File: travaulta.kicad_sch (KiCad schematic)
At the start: 26 parts, among them SW38 BOOT0, U1 STM32F411CCUx, U2 XC6206PxxxMR, Y1 16 MHz

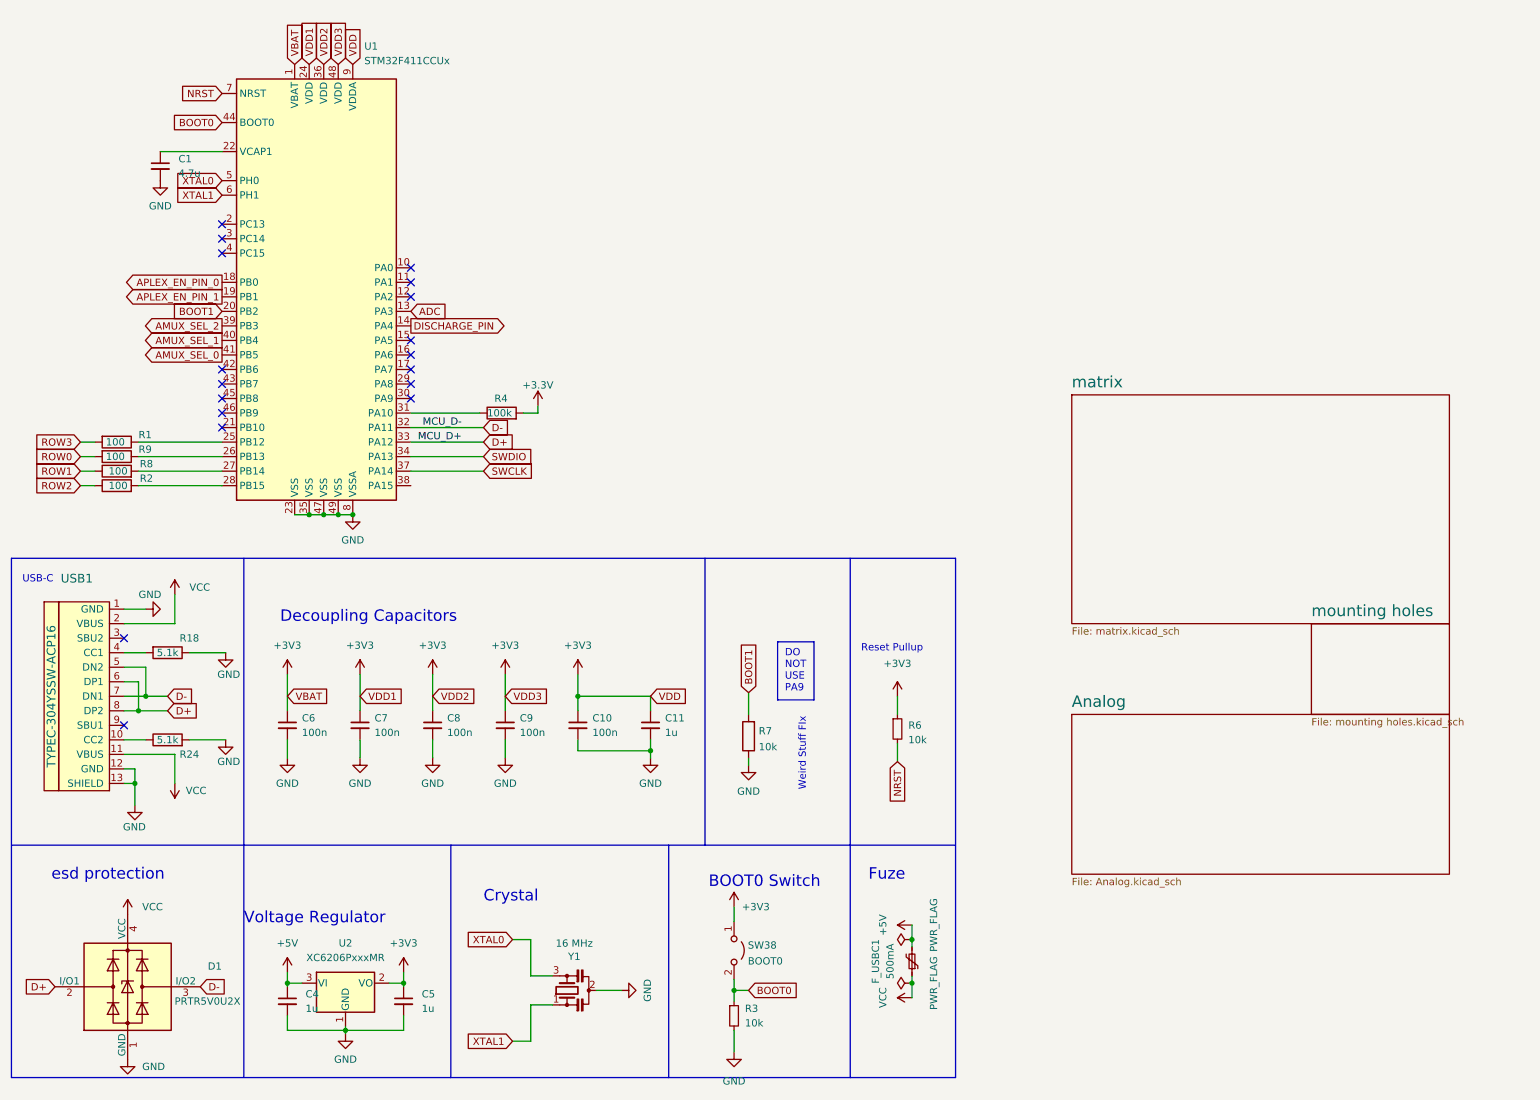
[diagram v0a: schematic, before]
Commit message: MCU swap, UCB components moved, crystal swap
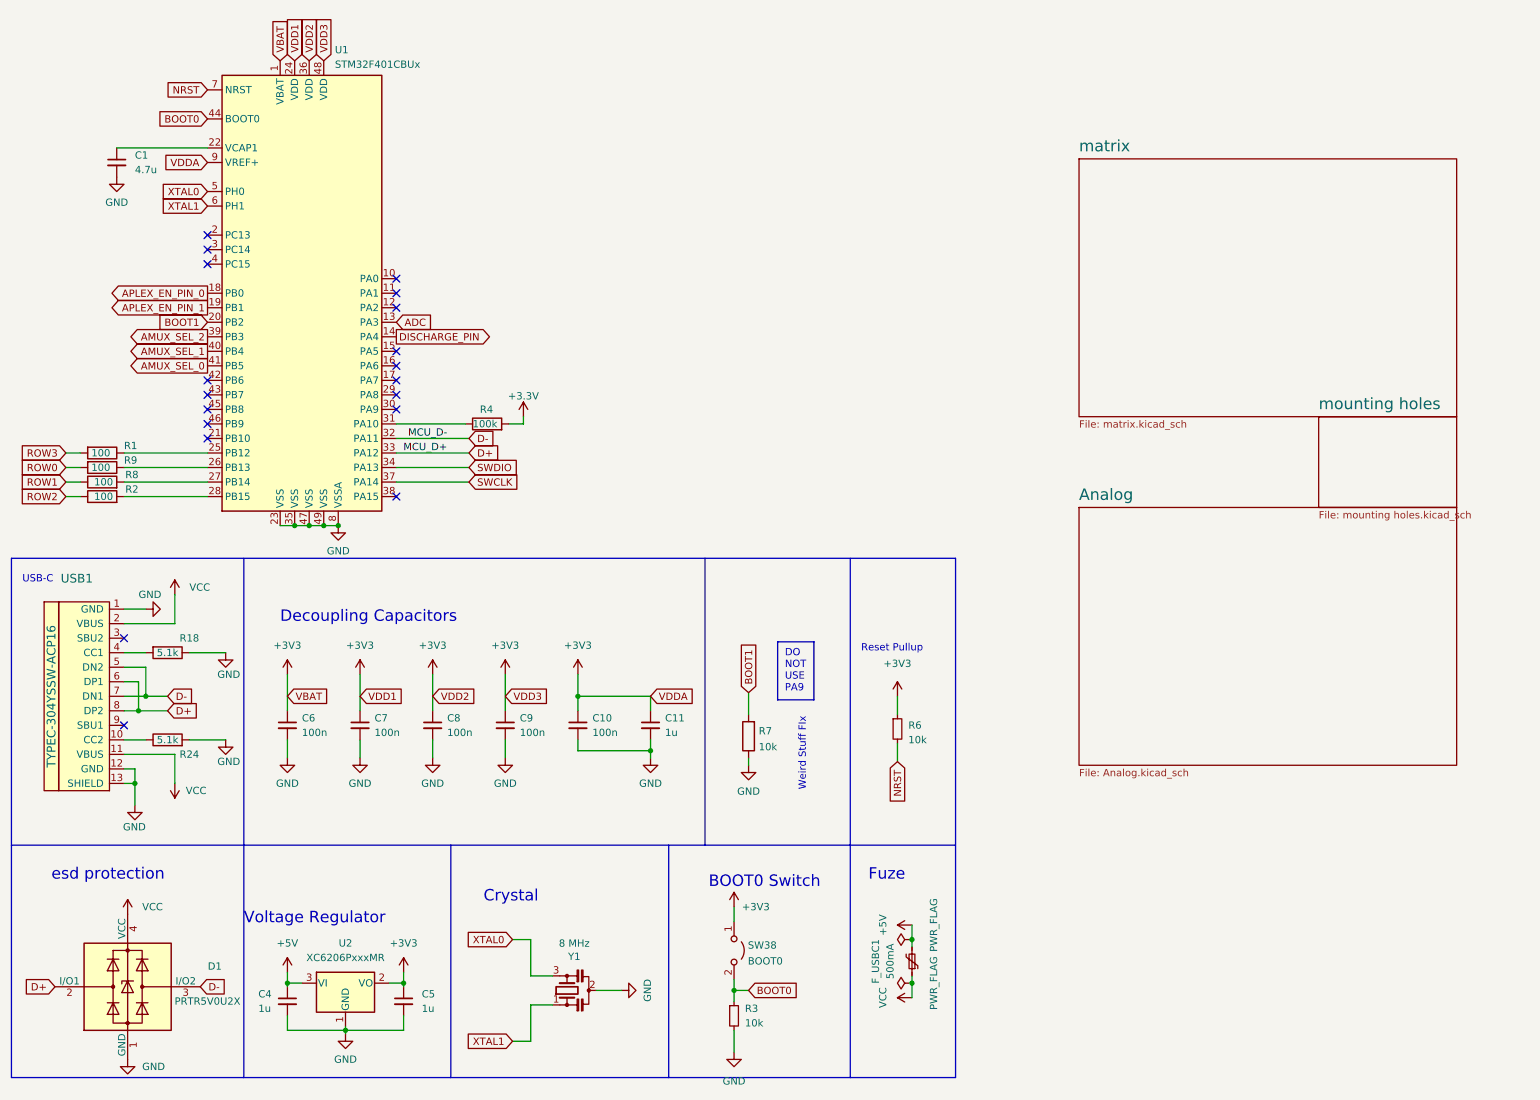
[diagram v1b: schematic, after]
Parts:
- removed U1: STM32F411CCUx, Package_DFN_QFN:QFN-48-1EP_7x7mm_P0.5mm_EP5.6x5.6mm, symbol MCU_ST_STM32F4:STM32F411CCUx
- added U1: STM32F401CBUx, Package_DFN_QFN:QFN-48-1EP_7x7mm_P0.5mm_EP5.6x5.6mm, symbol MCU_ST_STM32F4:STM32F401CBUx
- Y1: value 16 MHz -> 8 MHz
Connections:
- net +3V3: now also U1.1 (VBAT), U1.24 (VDD), U1.36 (VDD), U1.48 (VDD), U1.9 (VREF+)
- net ADC: now also U1.13 (PA3)
- net AMUX_SEL_0: now also U1.41 (PB5)
- net AMUX_SEL_1: now also U1.40 (PB4)
- net AMUX_SEL_2: now also U1.39 (PB3)
- net APLEX_EN_PIN_0: now also U1.18 (PB0)
- net APLEX_EN_PIN_1: now also U1.19 (PB1)
- net BOOT0: now also U1.44 (BOOT0)
- net BOOT1: now also U1.20 (PB2)
- net D+: now also U1.33 (PA12)
- net D-: now also U1.32 (PA11)
- net DISCHARGE_PIN: now also U1.14 (PA4)
- net GND: now also U1.23 (VSS), U1.35 (VSS), U1.47 (VSS), U1.49 (VSS), U1.8 (VSSA)
- net NRST: now also U1.7 (NRST)
- net SWCLK: now also U1.37 (PA14)
- net SWDIO: now also U1.34 (PA13)
- net XTAL0: now also U1.5 (PH0)
- net XTAL1: now also U1.6 (PH1)
- net at R4.1: now also U1.31 (PA10)
- net at R1.1: now also U1.25 (PB12)
- net at C1.1: now also U1.22 (VCAP1)
- net at R2.2: now also U1.28 (PB15)
- net at R9.1: now also U1.26 (PB13)
- net at R8.2: now also U1.27 (PB14)
- no-connect marks 18 -> 19
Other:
- moved on the sheet: C1, R1, R2, R4, R8, R9

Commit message: changed reset button, new production files
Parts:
- SW38: footprint Connector_PinHeader_2.54mm:PinHeader_1x02_P2.54mm_Vertical -> Button_Switch_SMD:SW_Push_SPST_NO_Alps_SKRK
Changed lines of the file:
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@@
       (effects (font (size 1.27 1.27)) (justify left))
     )
-    (property "Footprint" "Connector_PinHeader_2.54mm:PinHeader_1x02_P2.54mm_Vertical" (at 138.43 175.895 0)
+    (property "Footprint" "Button_Switch_SMD:SW_Push_SPST_NO_Alps_SKRK" (at 138.43 175.895 0)
       (effects (font (size 1.27 1.27)) hide)
     )
